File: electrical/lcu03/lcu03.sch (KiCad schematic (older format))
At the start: 94 parts, among them P1 screw, P10 swd, P11 stepper_conn, P12 stepper_conn, P13 stepper_conn, P16 screw, P17 screw, P2 screw, P3 screw, P4 screw, P5 ext-1, P6 ~rst~, P7 mode, P8 ext-2, P9 USB_B, Q1 bc857, Q2 bc847, Q3 bc857, Q4 ntd18n06l, U1 crystal-4pin, U2 CP2102, U3 m24c02, U4 NCP3063, U6 ts881, U7 lb1930mc

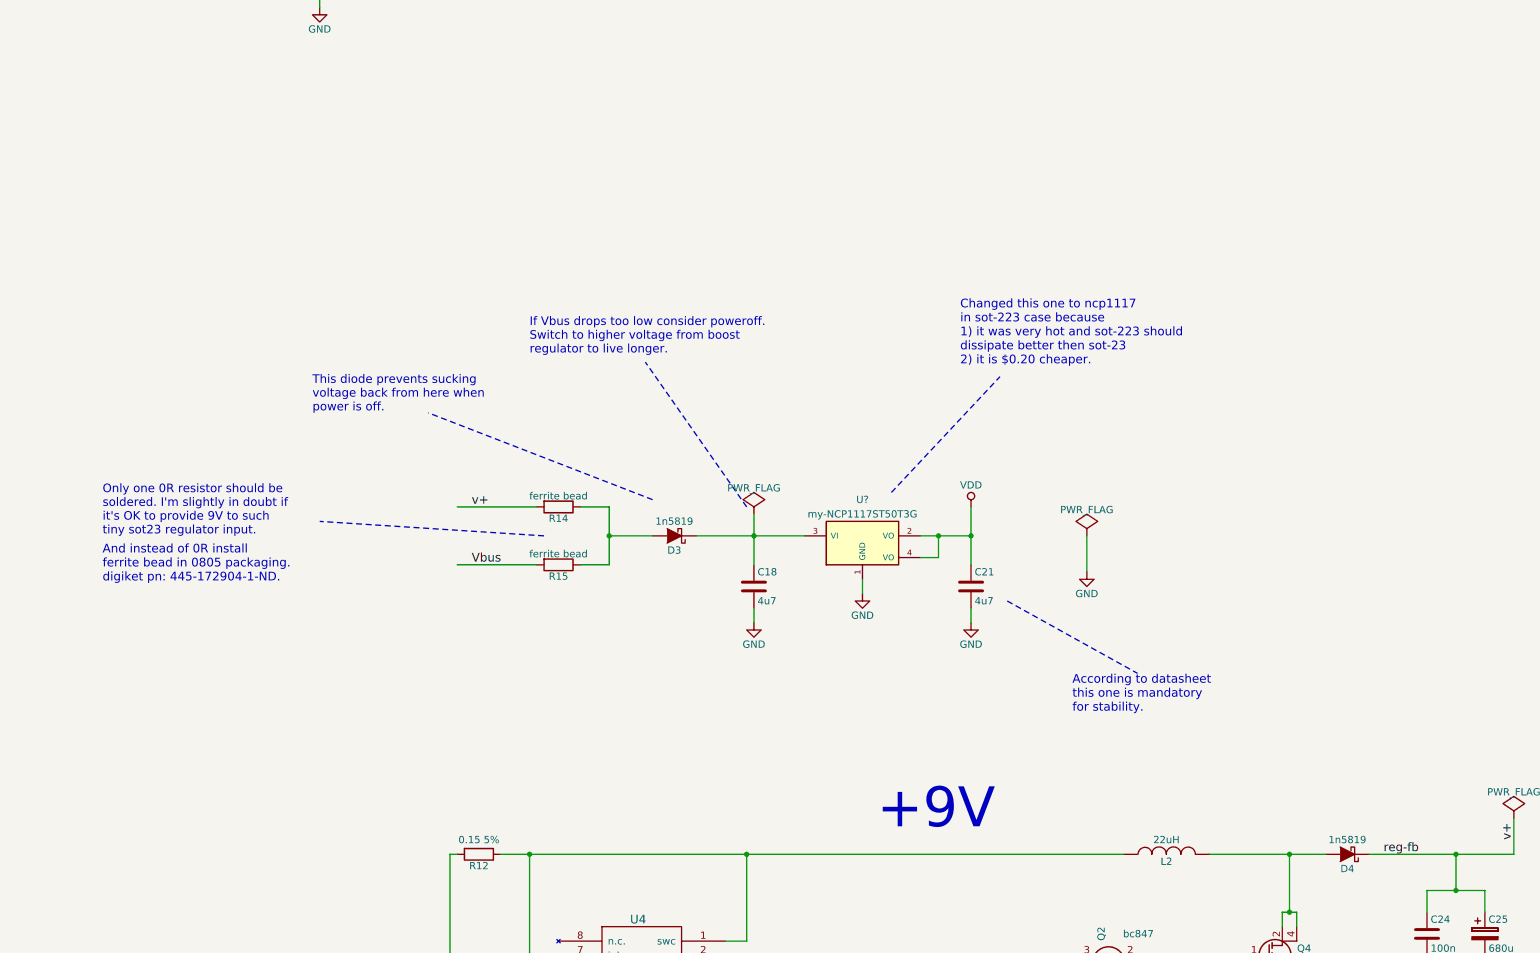
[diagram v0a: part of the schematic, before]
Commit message: Finished routing. Going to apply a few beautifications.
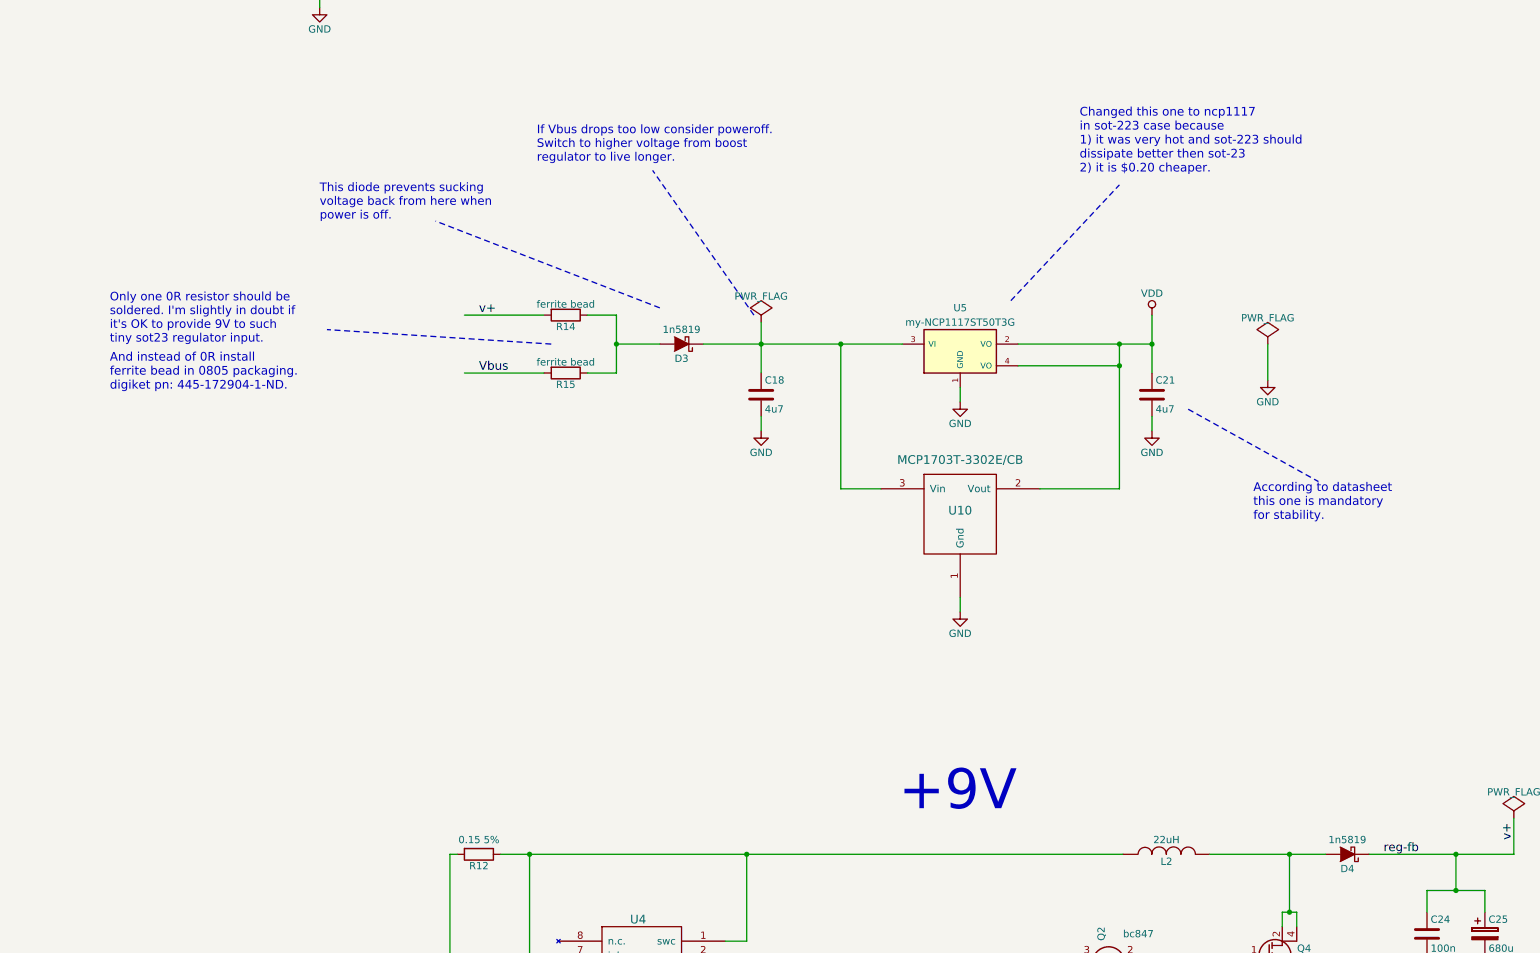
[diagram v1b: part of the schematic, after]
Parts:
- added U10: MCP1703T-3302E/CB, symbol MCP1703T-3302E/CB
- U5: renamed from U?; footprint (none) -> TO_SOT_Packages_SMD:SOT-223
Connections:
- wire segments 368 -> 372
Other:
- moved on the sheet: C18, C21, D3, R14, R15, U5

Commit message: Finished beautifications. Generated gerber files.
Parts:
- U10: footprint (none) -> TO_SOT_Packages_SMD:SOT-23
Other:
- note added: "This one is for backward compatibility. \nAs it is known that with it board worked. \nIf new stabilizer causes problems it could \nbe replaced with this one without PCB \nredesign."
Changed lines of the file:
@@
 F 0 "U10" H 15975 16925 60  0000 C CNN
 F 1 "MCP1703T-3302E/CB" H 15975 17275 60  0000 C CNN
-F 2 "" H 15975 16975 60  0000 C CNN
+F 2 "TO_SOT_Packages_SMD:SOT-23" H 15975 16975 60  0001 C CNN
 F 3 "" H 15975 16975 60  0000 C CNN
 	1    15975 16975
@@
 Wire Wire Line
 	15975 17625 15975 17725
+Wire Notes Line
+	16450 17175 17800 17900
+Text Notes 17875 18150 0    60   ~ 0
+This one is for backward compatibility. \nAs it is known that with it board worked. \nIf new stabilizer causes problems it could \nbe replaced with this one without PCB \nredesign.
 $EndSCHEMATC

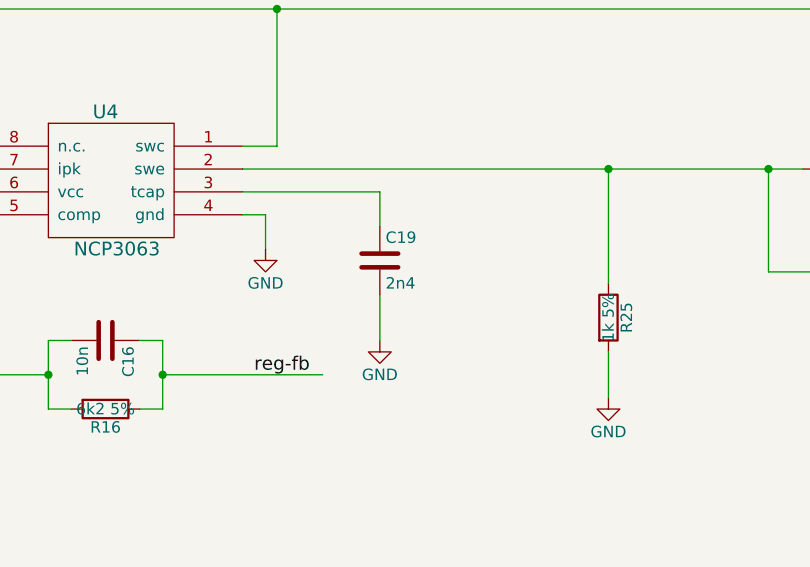
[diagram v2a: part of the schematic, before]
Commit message: Changed component value.
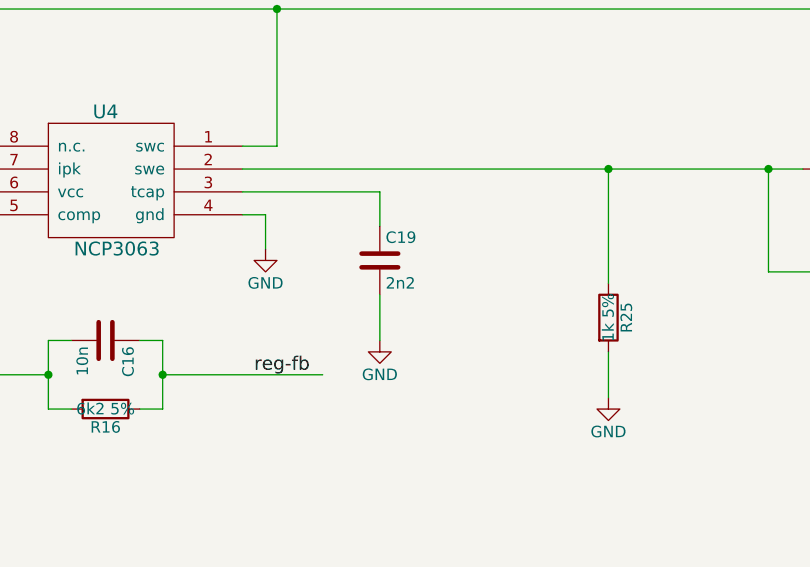
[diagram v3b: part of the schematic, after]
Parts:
- C19: value 2n4 -> 2n2
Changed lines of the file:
@@
 P 14950 20500
 F 0 "C19" H 14975 20600 50  0000 L CNN
-F 1 "2n4" H 14975 20400 50  0000 L CNN
+F 1 "2n2" H 14975 20400 50  0000 L CNN
 F 2 "Capacitors_SMD:C_0805" H 14988 20350 30  0001 C CNN
 F 3 "" H 14950 20500 60  0000 C CNN

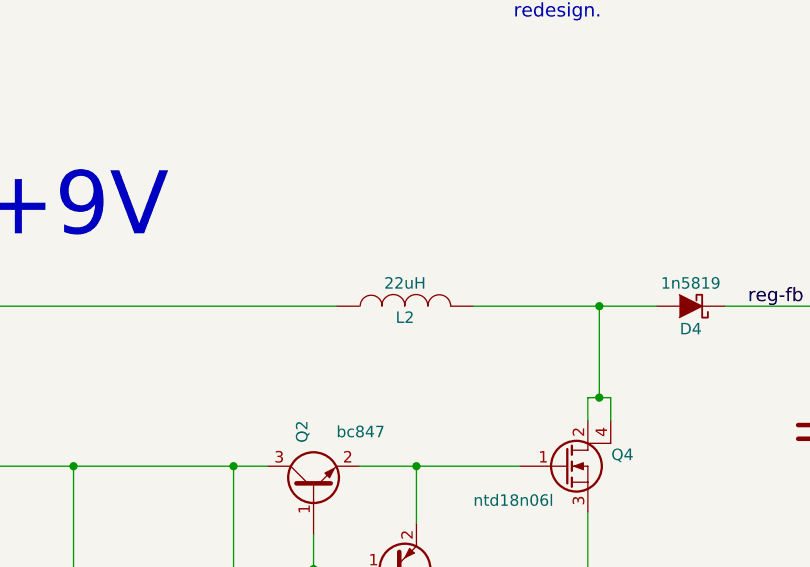
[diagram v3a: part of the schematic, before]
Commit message: Putting motors in reset mode when not spinning.
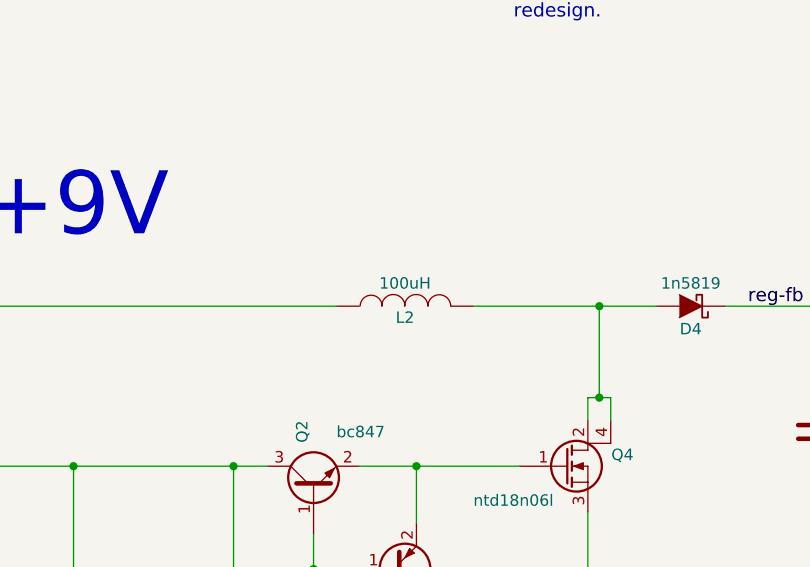
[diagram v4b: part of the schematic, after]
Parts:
- L2: value 22uH -> 100uH
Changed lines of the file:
@@
 P 17400 19400
 F 0 "L2" V 17350 19400 50  0000 C CNN
-F 1 "22uH" V 17500 19400 50  0000 C CNN
+F 1 "100uH" V 17500 19400 50  0000 C CNN
 F 2 "my-lib:my_inductance" H 17400 19400 60  0001 C CNN
 F 3 "" H 17400 19400 60  0000 C CNN

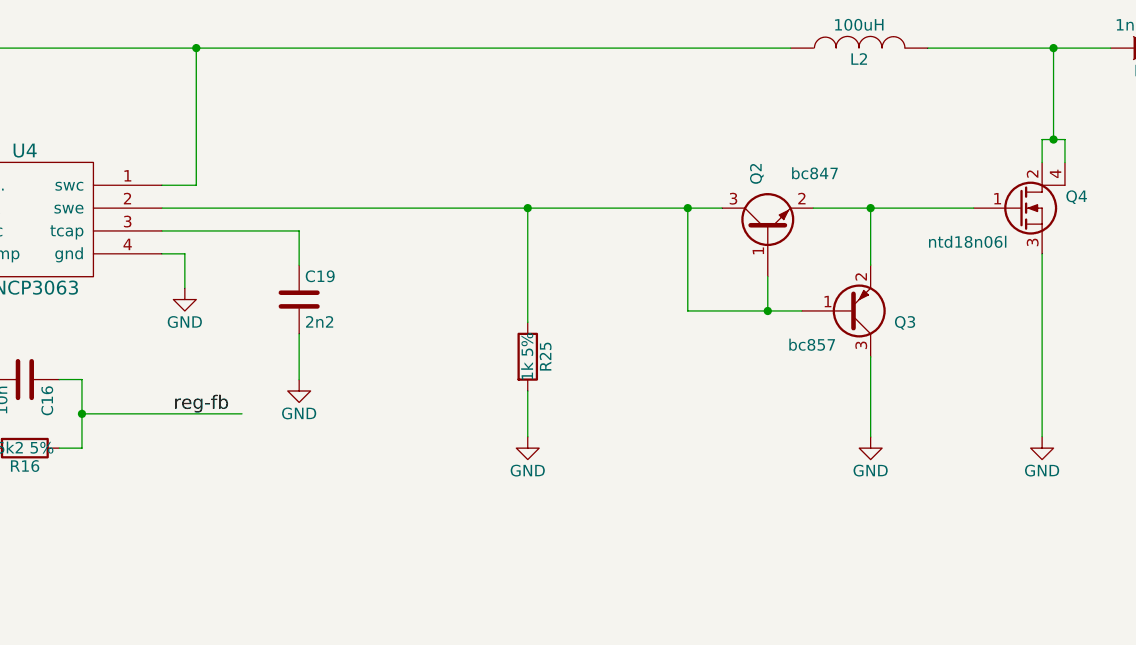
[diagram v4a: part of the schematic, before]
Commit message: Changed power supply circuit. Removed transistors and introduced 100R resistor in series.
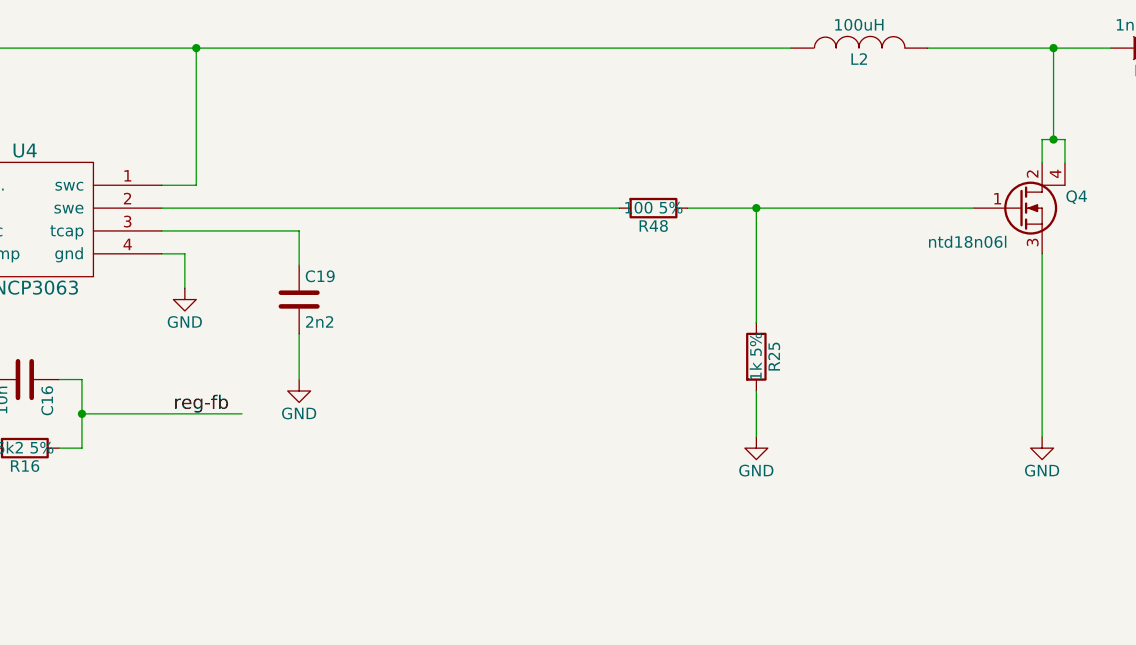
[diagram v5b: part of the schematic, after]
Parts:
- removed Q2: bc847, TO_SOT_Packages_SMD:SOT-23, symbol Q_NPN_BEC
- removed Q3: bc857, TO_SOT_Packages_SMD:SOT-23, symbol Q_PNP_BEC
- added R48: 100 5%, Resistors_SMD:R_0805, symbol R
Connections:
- wire segments 372 -> 367
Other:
- moved on the sheet: R25
